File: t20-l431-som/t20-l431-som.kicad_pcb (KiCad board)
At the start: 4 copper layers, 24 parts, among them U1 STM32L431-WLCSP64, U2 T20W80, U3 MX25U3232F

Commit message: Continued initial layout
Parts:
- added C20: 0.01 uF, azonenberg_pcb:EIA_0201_CAP_NOSILK, F.Cu at (90.3, 70.9)
- added C21: 1 uF, azonenberg_pcb:EIA_0201_CAP_NOSILK, F.Cu at (92.0, 71.6)
- added C22: 1 uF, azonenberg_pcb:EIA_0201_CAP_NOSILK, F.Cu at (92.0, 72.6)
- added C23: 1 uF, azonenberg_pcb:EIA_0201_CAP_NOSILK, F.Cu at (92.0, 72.1)
- added R1: 10K, azonenberg_pcb:EIA_0201_RES_NOSILK, F.Cu at (90.3, 70.2)
- added R2: 10K, azonenberg_pcb:EIA_0201_RES_NOSILK, F.Cu at (90.4, 73.3)
- added R3: 10K, azonenberg_pcb:EIA_0201_RES_NOSILK, F.Cu at (91.2, 70.9)
- added U4: MODULE_INTERNAL_T20_L431_HOST, azonenberg_pcb:MODULE_INTERNAL_T20_L431_HOST, F.Cu at (89.1, 73.3)
- added U5: LP3986TL-2518/NOPB, azonenberg_pcb:BGA_8_0.5MM_1.6MM_TI_YZR0008, F.Cu at (90.6, 72.1)
- moved C2 16.7 mm to (85.1, 77.4), turned to 0 degrees
- moved C4 15.3 mm to (88.1, 76.5), turned to 90 degrees
- moved U1 12.8 mm to (86.2, 75.4), turned to 180 degrees
- moved L1 12.3 mm to (83.8, 74.7), turned to -90 degrees
- moved C5 12.0 mm to (84.2, 74.7), turned to -90 degrees
- moved C3 9.16 mm to (87.2, 73.5), turned to 180 degrees
- moved C1 9.16 mm to (85.1, 73.5), turned to 180 degrees
- moved C7 0.32 mm to (89.2, 71.2), turned to -90 degrees
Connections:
- C7 pad 1: /3V3 -> /Power/3V3_FPGA
- C8 pad 1: /3V3 -> /Power/3V3_FPGA
- C9 pad 1: /3V3 -> /Power/3V3_FPGA
- U1 pad F2: unconnected-(U1B-PB15-PadF2) -> /CROSS_SPI_MOSI
- U1 pad G1: unconnected-(U1B-PB14-PadG1) -> /CROSS_SPI_MISO
- U1 pad G2: unconnected-(U1B-PB13-PadG2) -> /CROSS_SPI_SCK
- U1 pad G3: unconnected-(U1B-PB12-PadG3) -> /CROSS_SPI_CS_N
- U2 pad A2: unconnected-(U2C-GPIOL_74_PLLIN0-PadA2) -> /GPIOL_74_PLLIN0
- U2 pad B2: unconnected-(U2C-GPIOL_72_EXTFB0_CDI14-PadB2) -> /GPIOL_72
- U2 pad C1: unconnected-(U2C-GPIOL_69_CBSEL1-PadC1) -> /GPIOL_69_CBSEL1
- U2 pad D1: unconnected-(U2C-GPIOL_70_CBSEL0-PadD1) -> /GPIOL_70_CBSEL0
- U2 pad E1: unconnected-(U2C-GPIOL_71_NSTATUS-PadE1) -> /GPIOL_71_NSTATUS
- U2 pad E2: unconnected-(U2C-GPIOL_46-PadE2) -> /GPIOL_46
- U2 pad E7: unconnected-(U2F-GPIOR_76_PLLIN0-PadE7) -> /GPIOR_76_PLLIN0
- U2 pad F1: unconnected-(U2C-GPIOL_25_CLK1-PadF1) -> /GPIOL_25_CLK1
- U2 pad F6: /3V3 -> /Power/3V3_FPGA
- U2 pad G1: unconnected-(U2C-GPIOL_24_CLK0-PadG1) -> /GPIOL_24_CLK0
- U2 pad G2: unconnected-(U2C-GPIOL_20_CTRL0_CDI4-PadG2) -> /GPIOL_20_CTRL0_CDI4
- U2 pad G3: /3V3 -> /Power/3V3_FPGA
- U2 pad G5: /3V3 -> /Power/3V3_FPGA
- U2 pad G7: unconnected-(U2F-GPIOR_116_CTRL15-PadG7) -> /GPIOR_116_CTRL15
- U2 pad H1: unconnected-(U2C-GPIOL_13_CDI3-PadH1) -> /GPIOL_13_CDI3
- U2 pad H2: unconnected-(U2C-GPIOL_12_CDI2-PadH2) -> /GPIOL_12_CDI2
- U2 pad H5: unconnected-(U2F-GPIOR_117_CTRL14-PadH5) -> /GPIOR_117_CTRL14
- U2 pad H6: unconnected-(U2F-GPIOR_122_CLK13_CDI21-PadH6) -> /GPIOR_122_CLK13_CDI21
- U2 pad H7: unconnected-(U2G-GPIOR_133_CDI18-PadH7) -> /GPIOR_133_CDI18
- U2 pad H8: unconnected-(U2G-GPIOR_149_CBUS2-PadH8) -> /CROSS_SPI_MOSI
- U2 pad J5: unconnected-(U2F-GPIOR_123_CLK12_CDI20-PadJ5) -> /GPIOR_123_CLK12_CDI20
- U2 pad J6: unconnected-(U2G-GPIOR_154-PadJ6) -> /GPIOR_154
- U2 pad J7: unconnected-(U2G-GPIOR_151_CBUS0-PadJ7) -> /CROSS_SPI_CS_N
- U2 pad J8: unconnected-(U2G-GPIOR_150_CBUS1-PadJ8) -> /CROSS_SPI_SCK
- U2 pad K6: unconnected-(U2G-GPIOR_155-PadK6) -> /GPIOR_155
- U2 pad K7: unconnected-(U2G-GPIOR_158_TEST_N-PadK7) -> /CROSS_SPI_MISO
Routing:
- net /Power/2V5: track 1.32 -> 14.6 mm, vias 2 -> 3
- net /Power/3V3_FPGA: track 0.00 -> 8.30 mm, vias 0 -> 6
- net /GND: track 31.5 -> 38.7 mm, vias 28 -> 35
- net /3V3: track 10.7 -> 3.53 mm, vias 11 -> 6
- net /1V8: track 4.39 -> 7.71 mm, vias 4 -> 7
- net /CROSS_SPI_MISO: track 0.00 -> 2.70 mm
- net /1V8_EN: track 0.00 -> 2.51 mm, vias 0 -> 1
- net /CROSS_SPI_CS_N: track 0.00 -> 2.38 mm, vias 0 -> 1
- net /CROSS_SPI_SCK: track 0.00 -> 1.88 mm, vias 0 -> 1
- net /FPGA_RESET_N_1V8: track 0.78 -> 2.62 mm
- net /GPIOL_74_PLLIN0: track 0.00 -> 1.77 mm, vias 0 -> 1
- net /GPIOL_12_CDI2: track 0.00 -> 1.77 mm, vias 0 -> 1
- net /CROSS_SPI_MOSI: track 0.00 -> 1.73 mm, vias 0 -> 1
- net /GPIOL_13_CDI3: track 0.00 -> 1.71 mm, vias 0 -> 1
- net unconnected-(U2F-GPIOR_76_PLLIN0-PadE7): track 1.68 -> 0.00 mm
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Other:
- board outline added: 10.6 x 13 mm

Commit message: Continued initial layout
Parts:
- added C24: 1 uF, azonenberg_pcb:EIA_0201_CAP_NOSILK, F.Cu at (83.5, 75.8)
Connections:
- net /GPIOL_12_CDI2 renamed /FPGA IO/GPIOL_12_CDI2
- net /GPIOL_13_CDI3 renamed /FPGA IO/GPIOL_13_CDI3
- net /GPIOL_20_CTRL0_CDI4 renamed /FPGA IO/GPIOL_20_CTRL0_CDI4
- net /GPIOL_24_CLK0 renamed /FPGA IO/GPIOL_24_CLK0
- net /GPIOL_25_CLK1 renamed /FPGA IO/GPIOL_25_CLK1
- net /GPIOL_46 renamed /FPGA IO/GPIOL_46
- net /GPIOL_69_CBSEL1 renamed /FPGA IO/GPIOL_69_CBSEL1
- net /GPIOL_70_CBSEL0 renamed /FPGA IO/GPIOL_70_CBSEL0
- net /GPIOL_71_NSTATUS renamed /FPGA IO/GPIOL_71_NSTATUS
- net /GPIOL_72 renamed /FPGA IO/GPIOL_72
- net /GPIOL_74_PLLIN0 renamed /FPGA IO/GPIOL_74_PLLIN0
- net /GPIOR_116_CTRL15 renamed /FPGA IO/GPIOR_116_CTRL15
- net /GPIOR_117_CTRL14 renamed /FPGA IO/GPIOR_117_CTRL14
- net /GPIOR_122_CLK13_CDI21 renamed /FPGA IO/GPIOR_122_CLK13_CDI21
- net /GPIOR_123_CLK12_CDI20 renamed /FPGA IO/GPIOR_123_CLK12_CDI20
- net /GPIOR_76_PLLIN0 renamed /FPGA IO/GPIOR_76_PLLIN0
- U1 pad A2: unconnected-(U1A-PA15-PadA2) -> /MCU_TDI
- U1 pad A5: unconnected-(U1B-PB3-PadA5) -> /MCU_TDO
- U1 pad B2: unconnected-(U1A-PA14-PadB2) -> /MCU_TCK
- U1 pad B6: unconnected-(U1B-PB9-PadB6) -> /PB9
- U1 pad B7: /VBAT -> /Power/VBAT
- U1 pad C2: unconnected-(U1A-PA13-PadC2) -> /MCU_TMS
- U1 pad C5: unconnected-(U1E-BOOT0-PadC5) -> /MCU_BOOT0
- U1 pad D6: unconnected-(U1E-NRST-PadD6) -> /MCU_RST_N
- U1 pad D8: unconnected-(U1E-PH0-PadD8) -> /PH0
- U1 pad E5: unconnected-(U1A-PA4-PadE5) -> /PA4
- U1 pad E7: unconnected-(U1C-PC2-PadE7) -> /PC2
- U1 pad E8: unconnected-(U1C-PC1-PadE8) -> /PC1
- U1 pad F3: unconnected-(U1C-PC8-PadF3) -> /PC8
- U1 pad F4: unconnected-(U1B-PB0-PadF4) -> /PB0
- U1 pad F5: unconnected-(U1A-PA5-PadF5) -> /PA5
- U1 pad F6: unconnected-(U1A-PA2-PadF6) -> /PA2
- U1 pad F7: unconnected-(U1A-PA0-PadF7) -> /PA0
- U1 pad G4: unconnected-(U1B-PB2-PadG4) -> /PB2
- U1 pad G5: unconnected-(U1A-PA6-PadG5) -> /PA6
- U1 pad G6: unconnected-(U1A-PA3-PadG6) -> /PA3
- U1 pad G7: unconnected-(U1A-PA1-PadG7) -> /PA1
- U1 pad H3: unconnected-(U1B-PB11-PadH3) -> /PB11
- U1 pad H4: unconnected-(U1B-PB10-PadH4) -> /PB10
- U1 pad H5: unconnected-(U1B-PB1-PadH5) -> /PB1
- U1 pad H6: unconnected-(U1A-PA7-PadH6) -> /PA7
- U2 pad E8: unconnected-(U2F-GPIOR_81_MREFCLK-PadE8) -> /FPGA IO/GPIOR_81_MREFCLK
- U2 pad F7: unconnected-(U2F-GPIOR_77_PLLIN1-PadF7) -> /FPGA IO/FPGA_CLK_16MHZ
- U2 pad F8: unconnected-(U2F-GPIOR_78_EXTFB0_CDI31-PadF8) -> /FPGA IO/GPIOR_78_EXTFB0_CDI31
- U2 pad G6: unconnected-(U2F-GPIOR_79_EXTFB1_CDI30-PadG6) -> /FPGA IO/GPIOR_79_EXTFB1_CDI30
- U2 pad G8: unconnected-(U2G-GPIOR_132_CDI19-PadG8) -> /GPIOR_132_CDI19
- U4 pad C1: (no net) -> /GND
- U4 pad D1: (no net) -> /GND
- U4 pad E1: (no net) -> /GND
- U4 pad F1: (no net) -> /GND
- U4 pad F3: (no net) -> /GND
- U4 pad F4: (no net) -> /FPGA IO/GPIOR_79_EXTFB1_CDI30
- U4 pad F5: (no net) -> /FPGA IO/GPIOR_81_MREFCLK
- U4 pad F8: (no net) -> /GND
- U4 pad G1: (no net) -> /PH0
- U4 pad G2: (no net) -> /PC1
- U4 pad G3: (no net) -> /PB10
- U4 pad G5: (no net) -> /FPGA IO/GPIOR_78_EXTFB0_CDI31
- U4 pad G6: (no net) -> /PB11
- U4 pad G7: (no net) -> /GPIOR_132_CDI19
- U4 pad G8: (no net) -> /GND
- U4 pad H1: (no net) -> /PA3
- U4 pad H2: (no net) -> /PB1
- U4 pad H3: (no net) -> /PA5
- U4 pad H4: (no net) -> /PA4
- U4 pad H5: (no net) -> /PA6
- U4 pad H6: (no net) -> /PB0
- U4 pad H7: (no net) -> /PC8
- U4 pad J1: (no net) -> /PA0
- U4 pad J2: (no net) -> /PA7
- U4 pad J3: (no net) -> /GND
- U4 pad J4: (no net) -> /3V3
- U4 pad J5: (no net) -> /PB2
- U4 pad J6: (no net) -> /GND
- U4 pad K1: (no net) -> /PA2
- U4 pad K3: (no net) -> /PA1
- U4 pad L1: (no net) -> /PC2
- U4 pad N3: (no net) -> /Power/VBAT
- U4 pad N4: (no net) -> /PB9
- U4 pad N6: (no net) -> /MCU_TCK
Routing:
- net /GND: track 38.7 -> 55.4 mm, vias 35 -> 41
- net /3V3: track 3.53 -> 15.6 mm
- net /PH0: track 0.00 -> 5.03 mm, vias 0 -> 1
- net /PC1: track 0.00 -> 4.74 mm, vias 0 -> 1
- net /CROSS_SPI_MOSI: track 1.73 -> 6.13 mm, vias 1 -> 2
- net /FPGA IO/FPGA_CLK_16MHZ: track 0.00 -> 3.98 mm, vias 0 -> 2
- net /PA3: track 0.00 -> 3.70 mm, vias 0 -> 1
- net /PB1: track 0.00 -> 3.51 mm, vias 0 -> 1
- net /PB10: track 0.00 -> 3.30 mm, vias 0 -> 1
- net /PC8: track 0.00 -> 3.21 mm, vias 0 -> 2
- net /CROSS_SPI_CS_N: track 2.38 -> 5.59 mm, vias 1 -> 2
- net /PA2: track 0.00 -> 3.16 mm, vias 0 -> 1
- net /PA5: track 0.00 -> 3.02 mm, vias 0 -> 1
- net /PA7: track 0.00 -> 2.86 mm, vias 0 -> 1
- net /PA0: track 0.00 -> 2.76 mm, vias 0 -> 1
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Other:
- board size 10.6 x 13 mm -> 10.6 x 12.2 mm

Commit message: Continued STM32 fanout
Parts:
- added R4: 10K, azonenberg_pcb:EIA_0201_RES_NOSILK, F.Cu at (84.9, 78.5)
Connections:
- U1 pad A6: unconnected-(U1B-PB7-PadA6) -> /PB7
- U1 pad B8: unconnected-(U1C-PC13-PadB8) -> /PC13
- U1 pad C7: unconnected-(U1C-PC15-PadC7) -> /PC15
- U1 pad C8: unconnected-(U1C-PC14-PadC8) -> /PC14
- U1 pad D5: unconnected-(U1C-PC0-PadD5) -> /PC0
- U1 pad E6: unconnected-(U1C-PC3-PadE6) -> /PC3
- U2 pad F2: unconnected-(U2C-GPIOL_21_CTRL1_CDI5-PadF2) -> /FPGA IO/GPIOL_21_CTRL1_CDI5
- U4 pad A1: (no net) -> /GND
- U4 pad A2: (no net) -> /FPGA IO/GPIOL_21_CTRL1_CDI5
- U4 pad K1: /PA2 -> /PC2
- U4 pad K2: (no net) -> /PA2
- U4 pad L1: /PC2 -> /MCU_RST_N
- U4 pad M1: (no net) -> /GND
- U4 pad M2: (no net) -> /PC3
- U4 pad N1: (no net) -> /PC14
- U4 pad N2: (no net) -> /PC0
- U4 pad P1: (no net) -> /PC13
- U4 pad P2: (no net) -> /PC15
- U4 pad P3: (no net) -> /3V3
- U4 pad P4: (no net) -> /GND
- U4 pad R1: (no net) -> /PB7
- U4 pad R2: (no net) -> /MCU_TDO
- U4 pad R3: (no net) -> /MCU_BOOT0
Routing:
- net /3V3: track 15.6 -> 20.4 mm, vias 6 -> 7
- net /PB7: track 0.00 -> 4.08 mm, vias 0 -> 1
- net /GND: track 55.4 -> 59.2 mm, vias 41 -> 44
- net /FPGA IO/GPIOL_21_CTRL1_CDI5: track 0.00 -> 3.49 mm, vias 0 -> 2
- net /PC13: track 0.00 -> 2.89 mm, vias 0 -> 1
- net /MCU_TDO: track 0.63 -> 3.50 mm, vias 0 -> 1
- net unconnected-(U1C-PC12-PadA3): track 0.67 -> 3.48 mm
- net /PC15: track 0.00 -> 2.77 mm, vias 0 -> 1
- net /PC0: track 0.00 -> 2.63 mm, vias 0 -> 2
- net unconnected-(U1D-PD2-PadA4): track 0.63 -> 3.24 mm
- net /PC3: track 0.00 -> 2.27 mm, vias 0 -> 2
- net /PC14: track 0.00 -> 2.23 mm, vias 0 -> 1
- net unconnected-(U1C-PC0-PadD5): track 1.83 -> 0.00 mm, vias 1 -> 0
- net /MCU_BOOT0: track 1.53 -> 3.30 mm, vias 1 -> 2
- net unconnected-(U1C-PC15-PadC7): track 1.33 -> 0.00 mm, vias 1 -> 0
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
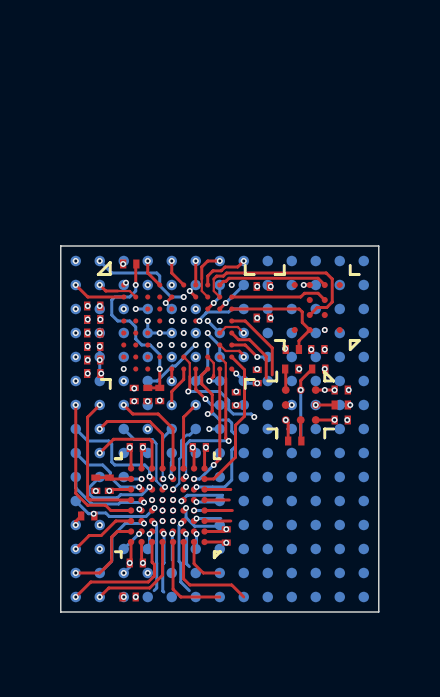
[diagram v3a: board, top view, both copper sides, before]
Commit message: Added oscillator
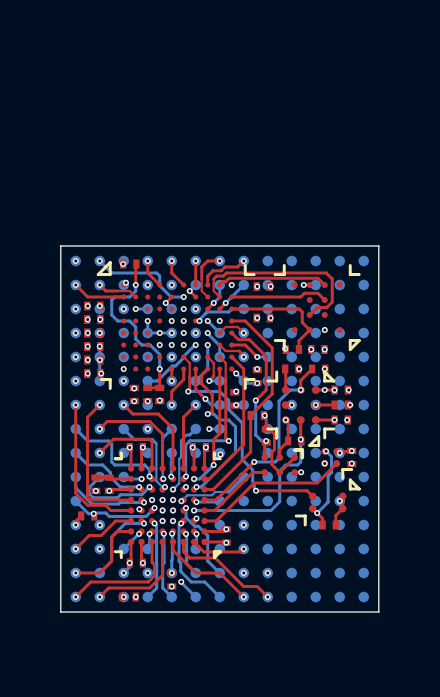
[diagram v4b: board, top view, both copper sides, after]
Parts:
- added C25: 1 uF, azonenberg_pcb:EIA_0201_CAP_NOSILK, F.Cu at (92.3, 73.8)
- added C26: 1 uF, azonenberg_pcb:EIA_0201_CAP_NOSILK, F.Cu at (91.5, 76.1)
- added R5: 10K, azonenberg_pcb:EIA_0201_RES_NOSILK, F.Cu at (86.3, 77.9)
- added R6: 10K, azonenberg_pcb:EIA_0201_RES_NOSILK, F.Cu at (89.2, 72.5)
- added R7: 10K, azonenberg_pcb:EIA_0201_RES_NOSILK, F.Cu at (89.5, 73.1)
- added U6: 74LVC1T45_DSBGA_YZP, azonenberg_pcb:BGA_6_1.5x0.9_0.5MM_TI_YZP, F.Cu at (89.9, 74.1)
- added U7: TPS22916BYFPR, azonenberg_pcb:BGA_4_0.4MM_0.8x0.8_TI_YFP0004, F.Cu at (91.6, 73.8)
- added U8: SIT8021AI-J4-XXS-16.000000, azonenberg_pcb:OSCILLATOR_SIT8021_WLCSP, F.Cu at (91.5, 75.3)
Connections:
- net /Power/3V3_FPGA renamed /3V3_FPGA
- U1 pad A3: unconnected-(U1C-PC12-PadA3) -> /PC12
- U1 pad A4: unconnected-(U1D-PD2-PadA4) -> /PD2
- U1 pad B3: unconnected-(U1C-PC11-PadB3) -> /PC11
- U1 pad B4: unconnected-(U1B-PB4-PadB4) -> /PB4_NJTRST
- U1 pad B5: unconnected-(U1B-PB6-PadB5) -> /PB6
- U1 pad C1: unconnected-(U1A-PA12-PadC1) -> /3V3_FPGA_EN
- U1 pad C3: unconnected-(U1C-PC10-PadC3) -> /PC10
- U1 pad C4: unconnected-(U1B-PB5-PadC4) -> /PB5
- U1 pad C6: unconnected-(U1B-PB8-PadC6) -> /PB8
- U1 pad D1: unconnected-(U1A-PA9-PadD1) -> /FPGA_DONE_3V3
- U1 pad D2: unconnected-(U1A-PA10-PadD2) -> /2V5_EN
- U1 pad D3: unconnected-(U1A-PA11-PadD3) -> /PA11
- U1 pad D4: unconnected-(U1C-PC4-PadD4) -> /PC4
- U1 pad E1: unconnected-(U1C-PC7-PadE1) -> /1V8_EN
- U1 pad E2: unconnected-(U1C-PC9-PadE2) -> /PC9
- U1 pad E3: unconnected-(U1A-PA8-PadE3) -> /PA8
- U1 pad E4: unconnected-(U1C-PC5-PadE4) -> /PC5
- U1 pad F1: unconnected-(U1C-PC6-PadF1) -> /FPGA_RESET_N_1V8
- U4 pad J12: (no net) -> /3V3
- U4 pad J7: (no net) -> /PC5
- U4 pad K8: (no net) -> /PA8
- U4 pad L12: (no net) -> /GND
- U4 pad L7: (no net) -> /PC9
- U4 pad M7: (no net) -> /GND
- U4 pad M8: (no net) -> /PC4
- U4 pad N7: (no net) -> /3V3
- U4 pad N8: (no net) -> /MCU_TDI
- U4 pad P5: (no net) -> /PB4_NJTRST
- U4 pad P6: (no net) -> /PC11
- U4 pad P7: (no net) -> /PA11
- U4 pad P8: (no net) -> /GND
- U4 pad P9: (no net) -> /3V3
- U4 pad R4: (no net) -> /PB8
- U4 pad R5: (no net) -> /PB6
- U4 pad R6: (no net) -> /PB5
- U4 pad R7: (no net) -> /PC10
- U4 pad R8: (no net) -> /PD2
- U4 pad R9: (no net) -> /PC12
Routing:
- net /3V3: track 20.4 -> 34.0 mm, vias 7 -> 12
- net /3V3_FPGA: track 8.30 -> 19.4 mm, vias 6 -> 8
- net /GND: track 59.2 -> 67.2 mm, vias 44 -> 48
- net /Power/1V2: track 14.1 -> 20.7 mm
- net /2V5_EN: track 0.65 -> 6.28 mm, vias 0 -> 2
- net /1V8: track 7.71 -> 13.0 mm, vias 7 -> 8
- net /3V3_FPGA_EN: track 0.00 -> 5.20 mm
- net /FPGA_RESET_N_1V8: track 2.62 -> 7.54 mm
- net /1V8_EN: track 2.51 -> 6.70 mm, vias 1 -> 2
- net /FPGA IO/FPGA_CLK_16MHZ: track 3.98 -> 8.08 mm
- net /PC12: track 0.00 -> 3.76 mm, vias 0 -> 1
- net unconnected-(U1C-PC12-PadA3): track 3.48 -> 0.00 mm
- net /PC10: track 0.00 -> 3.42 mm, vias 0 -> 1
- net /PD2: track 0.00 -> 3.28 mm, vias 0 -> 1
- net unconnected-(U1D-PD2-PadA4): track 3.24 -> 0.00 mm
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
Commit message: Deleted rightmost column of balls that werent doing anything
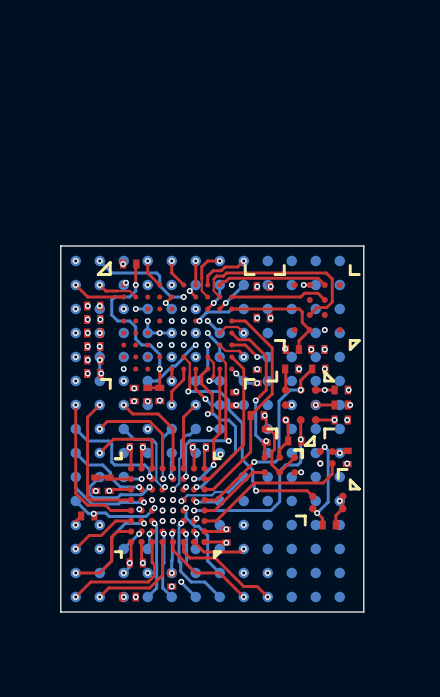
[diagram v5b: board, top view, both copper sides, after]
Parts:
- moved U4 1.65 mm to (87.5, 72.9)
- moved C25 0.15 mm to (92.2, 73.8)
- moved U7 0.15 mm to (91.5, 73.8)
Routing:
- net /Power/2V5: track 16.2 -> 14.0 mm
- net /3V3: vias 12 -> 11
- net /1V8: vias 8 -> 7
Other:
- board size 10.6 x 12.2 mm -> 10.1 x 12.2 mm

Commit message: Finished initial L431 SOM routing
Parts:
- added C27: 1 uF, azonenberg_pcb:EIA_0201_CAP_NOSILK, F.Cu at (90.9, 76.5)
- added C28: 1 uF, azonenberg_pcb:EIA_0201_CAP_NOSILK, F.Cu at (90.0, 77.8)
- added C29: 4.7 uF 2.5V, azonenberg_pcb:EIA_0201_CAP_NOSILK, F.Cu at (89.3, 77.1)
- added C30: 4.7 uF 2.5V, azonenberg_pcb:EIA_0201_CAP_NOSILK, F.Cu at (89.3, 76.2)
- added C31: 4.7 uF 2.5V, azonenberg_pcb:EIA_0201_CAP_NOSILK, F.Cu at (90.0, 76.0)
- added R8: 10K, azonenberg_pcb:EIA_0201_RES_NOSILK, F.Cu at (91.5, 74.5)
- added R9: 10K, azonenberg_pcb:EIA_0201_RES_NOSILK, F.Cu at (90.9, 77.0)
- added U9: NCP139AFCT120T2G, azonenberg_pcb:BGA_6_1.3x1.0_0.4MM, F.Cu at (90.0, 76.9)
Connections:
- U1 pad D3: /PA11 -> /1V2_EN
- U1 pad D7: unconnected-(U1E-PH1-PadD7) -> /PH1
- U4 pad B9: (no net) -> /GND
- U4 pad C9: (no net) -> /GND
- U4 pad L8: (no net) -> /3V3
- U4 pad M10: (no net) -> /GND
- U4 pad M9: (no net) -> /GND
- U4 pad N2: /PC0 -> /PH1
- U4 pad P10: (no net) -> /3V3
- U4 pad P7: /PA11 -> (no net)
- U4 pad P8: /GND -> /3V3
- U4 pad P9: /3V3 -> /GND
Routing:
- net /GND: track 67.2 -> 74.6 mm, vias 48 -> 53
- net /1V2_EN: track 0.00 -> 6.27 mm, vias 0 -> 2
- net /Power/1V2: track 20.7 -> 24.9 mm, vias 13 -> 16
- net /PA11: track 2.82 -> 0.00 mm, vias 1 -> 0
- net /3V3: track 34.0 -> 36.2 mm, vias 11 -> 15
- net /PH1: track 0.00 -> 2.19 mm, vias 0 -> 2
- net /PC0: track 2.63 -> 1.09 mm, vias 2 -> 1
- net unconnected-(U1E-PH1-PadD7): track 0.09 -> 0.00 mm, vias 1 -> 0

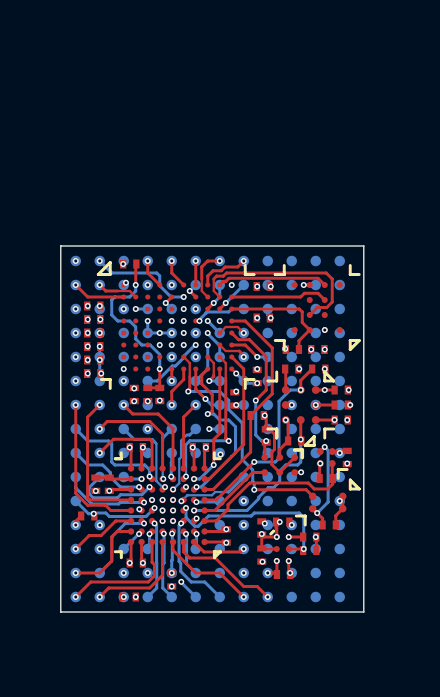
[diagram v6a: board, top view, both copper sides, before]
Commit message: Continued L431 SoM layout
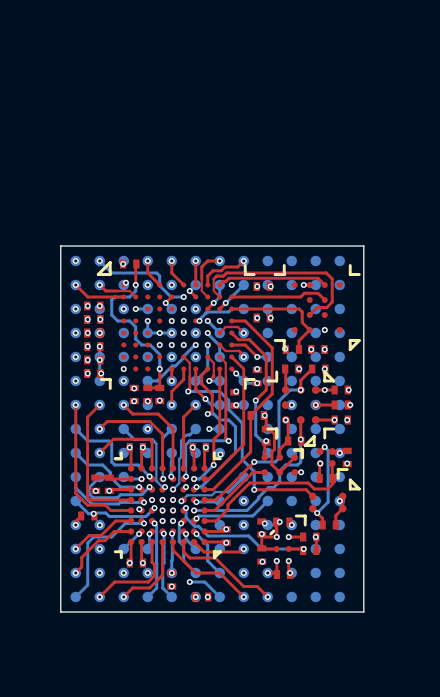
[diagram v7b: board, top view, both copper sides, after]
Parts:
- moved R4 2.42 mm to (87.3, 78.5)
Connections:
- U4 pad L9: (no net) -> /MCU_TMS
- U4 pad N6: /MCU_TCK -> /PC11
- U4 pad P2: /PC15 -> /PC0
- U4 pad P6: /PC11 -> /PC10
- U4 pad P7: (no net) -> /MCU_TCK
- U4 pad R1: /PB7 -> /PC15
- U4 pad R2: /MCU_TDO -> /PB7
- U4 pad R3: /MCU_BOOT0 -> /MCU_TDO
- U4 pad R6: /PB5 -> /MCU_BOOT0
- U4 pad R7: /PC10 -> /PB5
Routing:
- net /MCU_TMS: track 0.12 -> 2.73 mm
- net /PC0: track 1.09 -> 3.25 mm, vias 1 -> 2
- net /PC15: track 2.77 -> 4.25 mm
- net /PC10: track 3.42 -> 2.02 mm
- net /MCU_TCK: track 0.64 -> 1.75 mm
- net /1V2_EN: track 6.27 -> 5.29 mm
- net /PB7: track 4.08 -> 3.28 mm
- net /MCU_TDO: track 3.50 -> 2.70 mm
- net /PC11: track 1.55 -> 0.81 mm
- net /PB5: track 2.85 -> 3.47 mm
- added copper zone on In2.Cu, net /1V8
- added copper zone on In2.Cu, net /3V3
- added copper zone on In2.Cu, net /3V3_FPGA
- added copper zone on In1.Cu, net /GND
- added copper zone on In2.Cu, net /Power/2V5

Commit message: More work on T20-L431 module
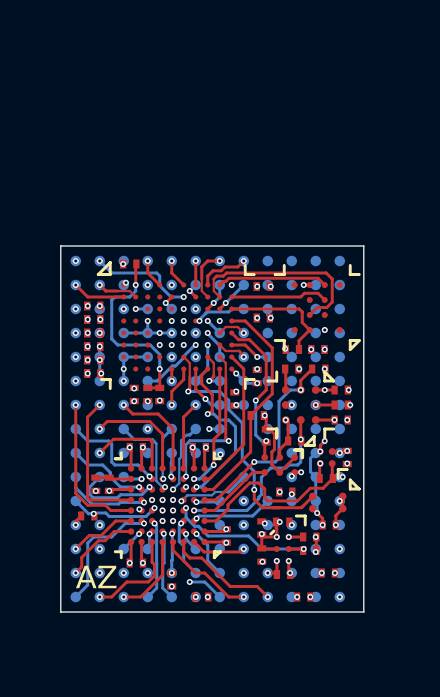
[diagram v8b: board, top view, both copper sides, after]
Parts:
- added C32: 1 uF, azonenberg_pcb:EIA_0201_CAP_NOSILK, F.Cu at (90.7, 78.5)
- added C33: 1 uF, azonenberg_pcb:EIA_0201_CAP_NOSILK, F.Cu at (90.1, 75.0)
- added C34: 1 uF, azonenberg_pcb:EIA_0201_CAP_NOSILK, F.Cu at (91.5, 77.7)
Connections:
- U4 pad D3: (no net) -> /GND
- U4 pad E3: (no net) -> /GND
- U4 pad E4: (no net) -> /GND
- U4 pad J11: (no net) -> /3V3_FPGA
- U4 pad K10: (no net) -> /3V3
- U4 pad K11: (no net) -> /3V3_FPGA
- U4 pad K12: (no net) -> /GND
- U4 pad L10: (no net) -> /GND
- U4 pad L11: (no net) -> /3V3_FPGA
- U4 pad M11: (no net) -> /3V3_FPGA
- U4 pad M12: (no net) -> /GND
- U4 pad N11: (no net) -> /GND
- U4 pad N12: (no net) -> /GND
- U4 pad P11: (no net) -> /GND
- U4 pad P12: (no net) -> /3V3
- U4 pad R10: (no net) -> /GND
- U4 pad R11: (no net) -> /3V3
- U4 pad R12: (no net) -> /GND
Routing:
- net /GND: track 74.8 -> 83.7 mm, vias 53 -> 61
- net /3V3: track 36.7 -> 40.5 mm, vias 15 -> 20
- net /FPGA IO/FPGA_CLK_16MHZ: track 8.10 -> 8.85 mm
- net /Power/2V5: track 14.0 -> 14.8 mm
- net /3V3_FPGA: track 18.9 -> 19.5 mm, vias 8 -> 10
- added copper zone on In2.Cu, net /Power/1V2
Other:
- board text added: "AZ"
